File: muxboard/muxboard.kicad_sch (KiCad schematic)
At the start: 5 parts, among them U1 ADG426BNZ, U2 ADG426BNZ, U3 ADG426BNZ, U4 ADG1204YRUZ

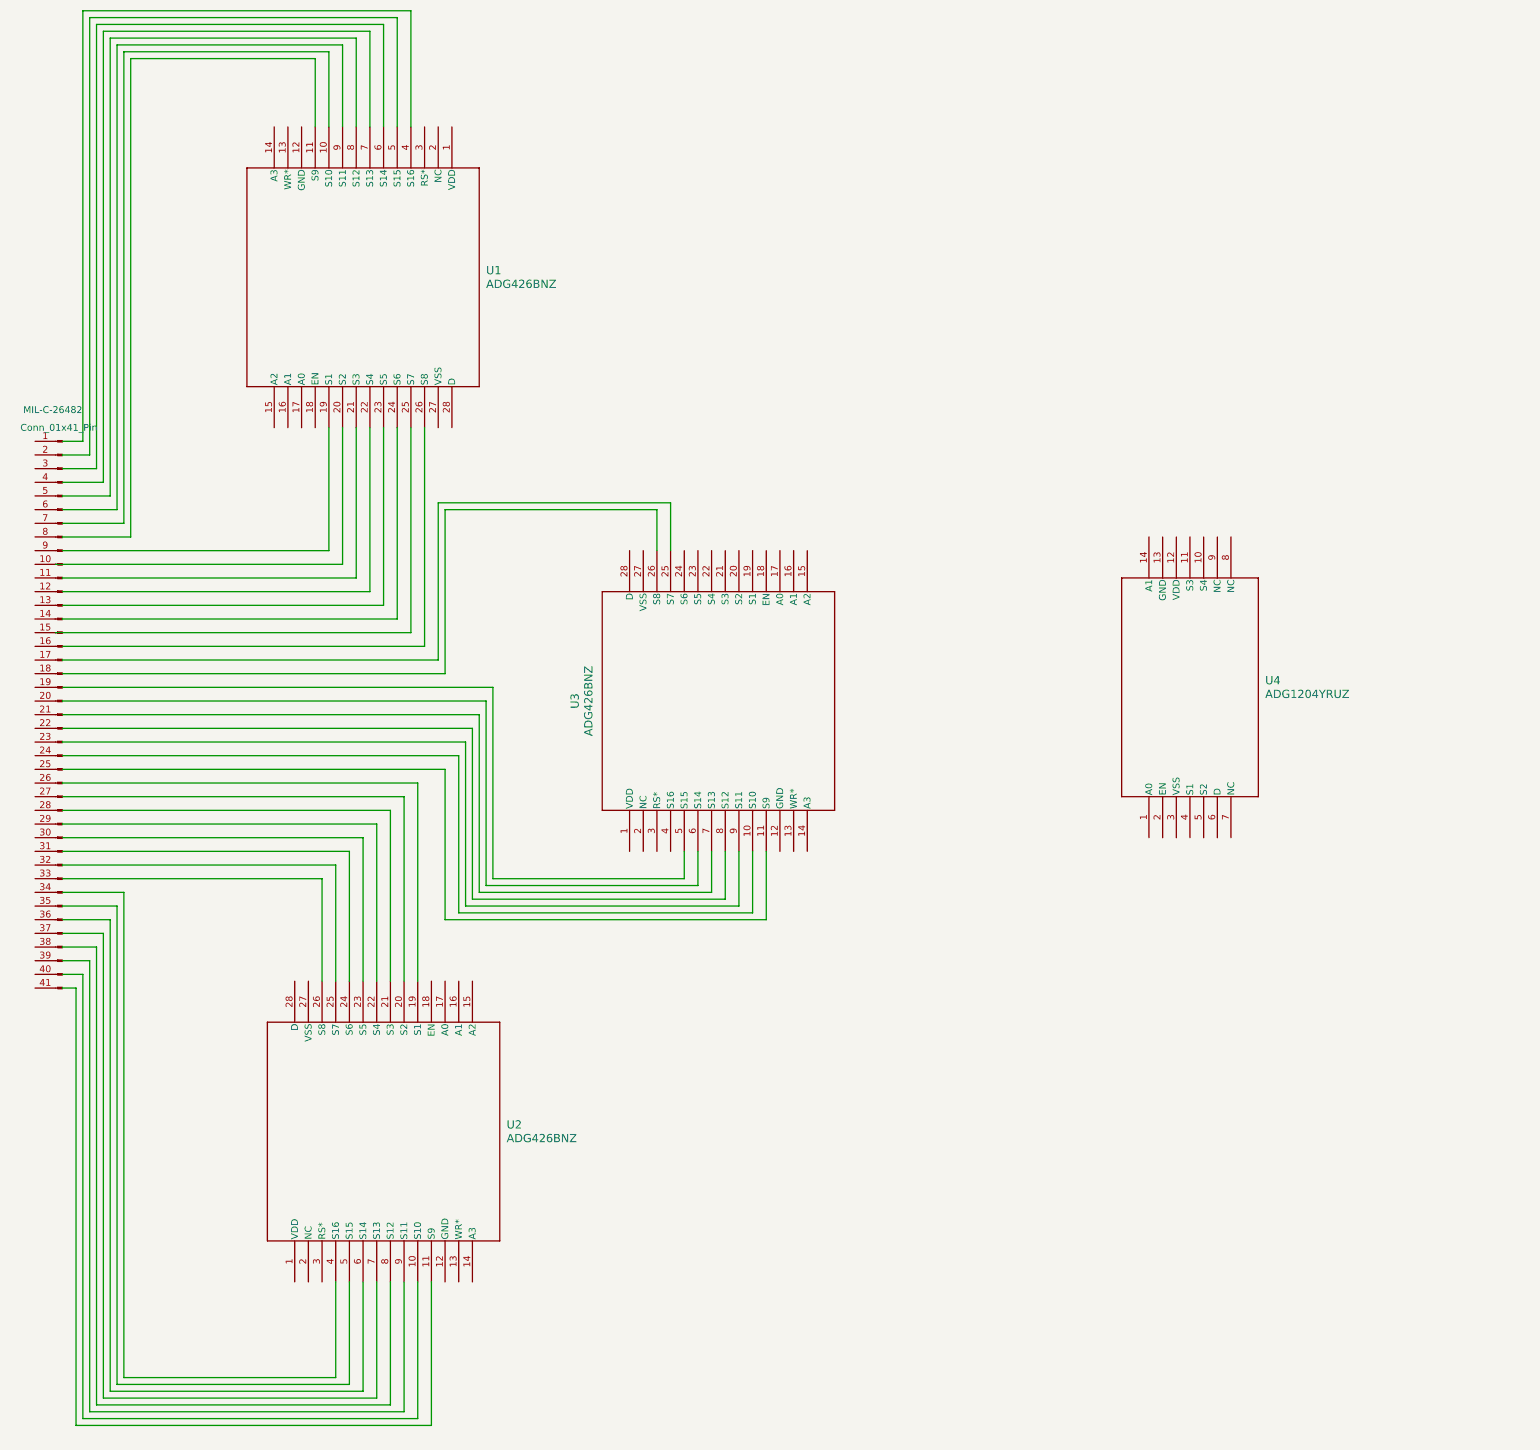
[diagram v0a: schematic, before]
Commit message: uploaded pcb terminal blocks; still need to connect and check wire connection
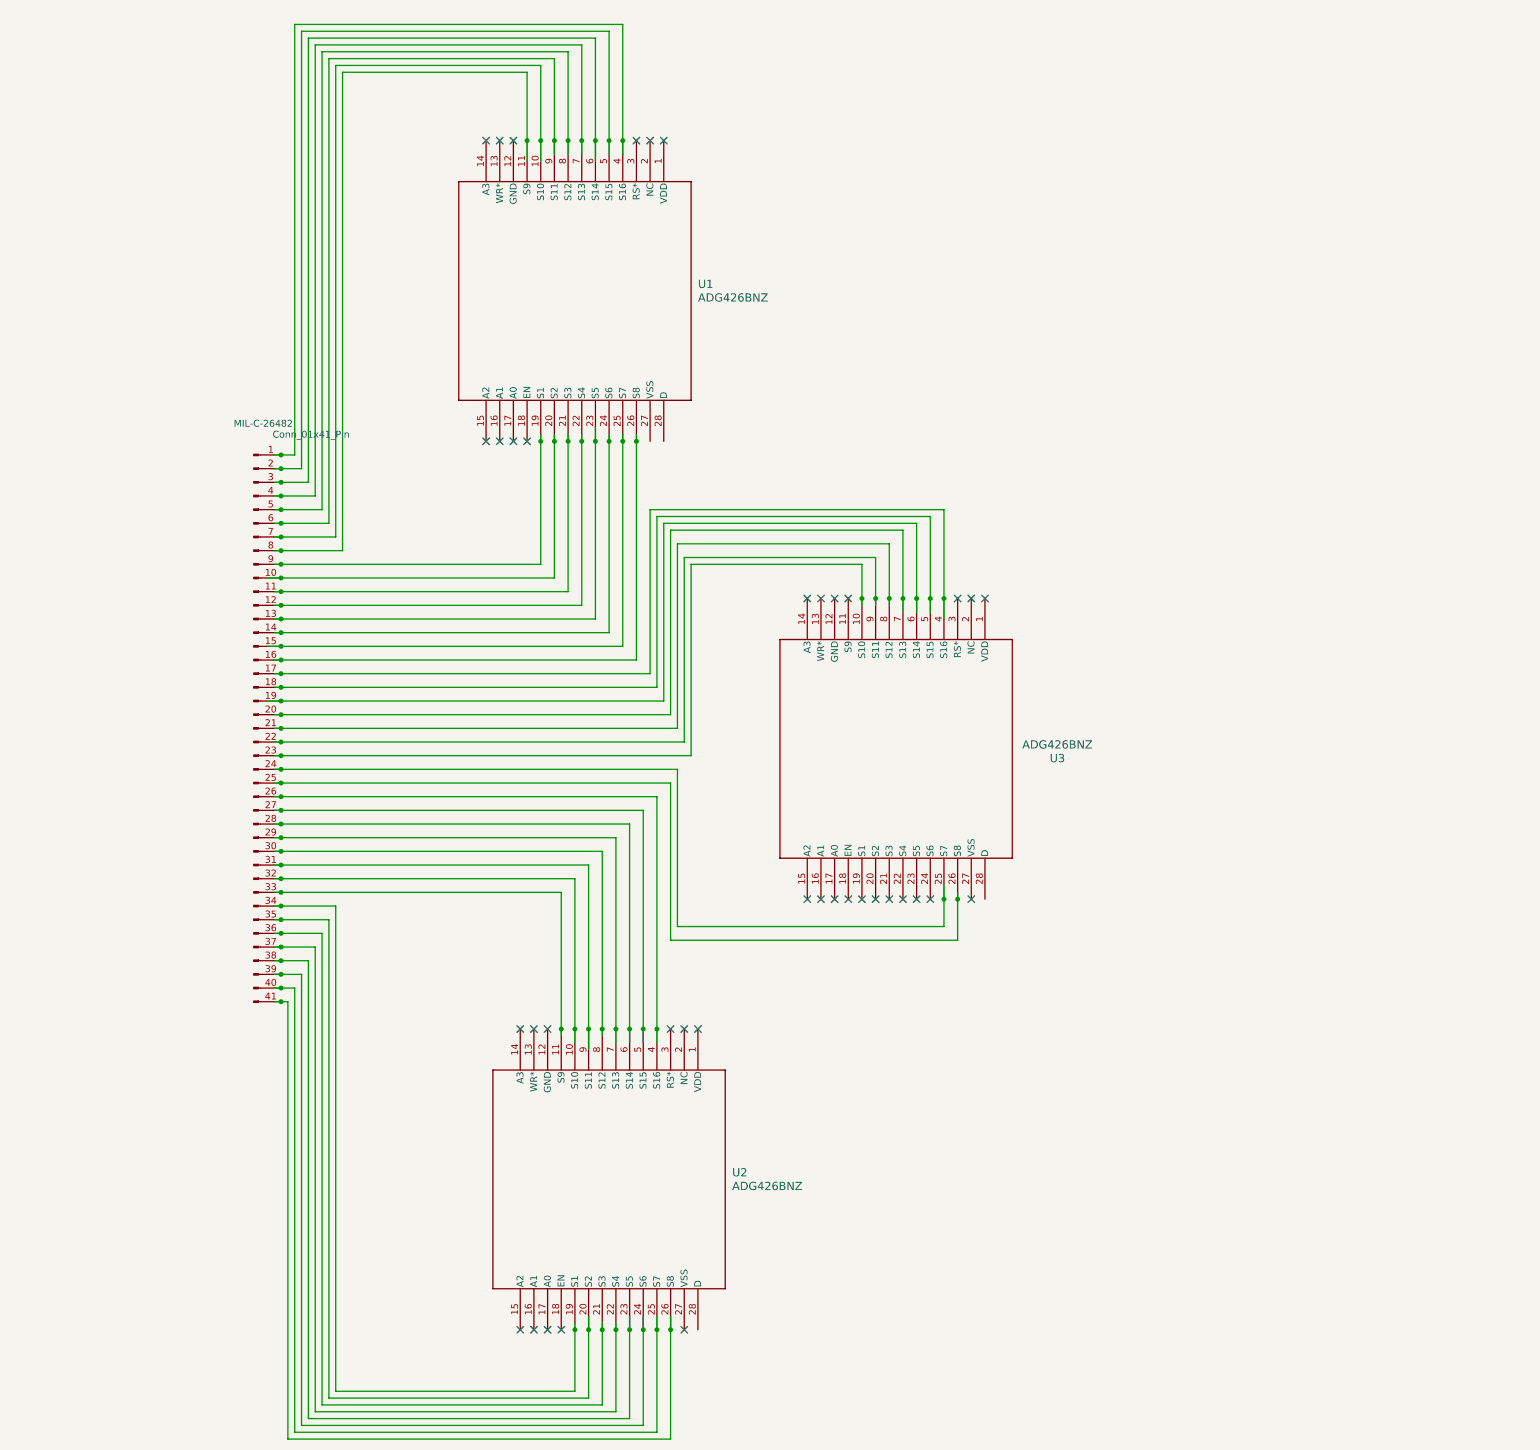
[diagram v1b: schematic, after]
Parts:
- removed U4: ADG1204YRUZ, RU_14_ADI, symbol ADG1204YRUZ:ADG1204YRUZ
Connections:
- net at MIL-C-26482.1 (Pin_1): now also U1.4 (S16)
- net at MIL-C-26482.10 (Pin_10): now also U1.20 (S2)
- net at MIL-C-26482.11 (Pin_11): now also U1.21 (S3)
- net at MIL-C-26482.12 (Pin_12): now also U1.22 (S4)
- net at MIL-C-26482.13 (Pin_13): now also U1.23 (S5)
- net at MIL-C-26482.14 (Pin_14): now also U1.24 (S6)
- net at MIL-C-26482.15 (Pin_15): now also U1.25 (S7)
- net at MIL-C-26482.16 (Pin_16): now also U1.26 (S8)
- net at MIL-C-26482.17 (Pin_17): now also U3.4 (S16)
- net at MIL-C-26482.18 (Pin_18): now also U3.5 (S15)
- net at MIL-C-26482.19 (Pin_19): now also U3.6 (S14)
- net at MIL-C-26482.2 (Pin_2): now also U1.5 (S15)
- net at MIL-C-26482.20 (Pin_20): now also U3.7 (S13)
- net at MIL-C-26482.21 (Pin_21): now also U3.8 (S12)
- net at MIL-C-26482.22 (Pin_22): now also U3.9 (S11)
- net at MIL-C-26482.23 (Pin_23): now also U3.10 (S10)
- net at MIL-C-26482.24 (Pin_24): now also U3.25 (S7)
- net at MIL-C-26482.25 (Pin_25): now also U3.26 (S8)
- net at MIL-C-26482.26 (Pin_26): now also U2.4 (S16)
- net at MIL-C-26482.27 (Pin_27): now also U2.5 (S15)
- net at MIL-C-26482.28 (Pin_28): now also U2.6 (S14)
- net at MIL-C-26482.29 (Pin_29): now also U2.7 (S13)
- net at MIL-C-26482.3 (Pin_3): now also U1.6 (S14)
- net at MIL-C-26482.30 (Pin_30): now also U2.8 (S12)
- net at MIL-C-26482.31 (Pin_31): now also U2.9 (S11)
- net at MIL-C-26482.32 (Pin_32): now also U2.10 (S10)
- net at MIL-C-26482.33 (Pin_33): now also U2.11 (S9)
- net at MIL-C-26482.34 (Pin_34): now also U2.19 (S1)
- net at MIL-C-26482.35 (Pin_35): now also U2.20 (S2)
- net at MIL-C-26482.36 (Pin_36): now also U2.21 (S3)
- net at MIL-C-26482.37 (Pin_37): now also U2.22 (S4)
- net at MIL-C-26482.38 (Pin_38): now also U2.23 (S5)
- net at MIL-C-26482.39 (Pin_39): now also U2.24 (S6)
- net at MIL-C-26482.4 (Pin_4): now also U1.7 (S13)
- net at MIL-C-26482.40 (Pin_40): now also U2.25 (S7)
- net at MIL-C-26482.41 (Pin_41): now also U2.26 (S8)
- net at MIL-C-26482.5 (Pin_5): now also U1.8 (S12)
- net at MIL-C-26482.6 (Pin_6): now also U1.9 (S11)
- net at MIL-C-26482.7 (Pin_7): now also U1.10 (S10)
- net at MIL-C-26482.8 (Pin_8): now also U1.11 (S9)
- net at MIL-C-26482.9 (Pin_9): now also U1.19 (S1)
- no-connect marks 0 -> 39
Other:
- moved on the sheet: MIL-C-26482, U1, U2, U3

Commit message: uploaded 3-pole terminal block; schematic rough draft is finished; left to do: - run ERC checks with connections - make sure all connections are properly aligned - ensure wire layout is feasible
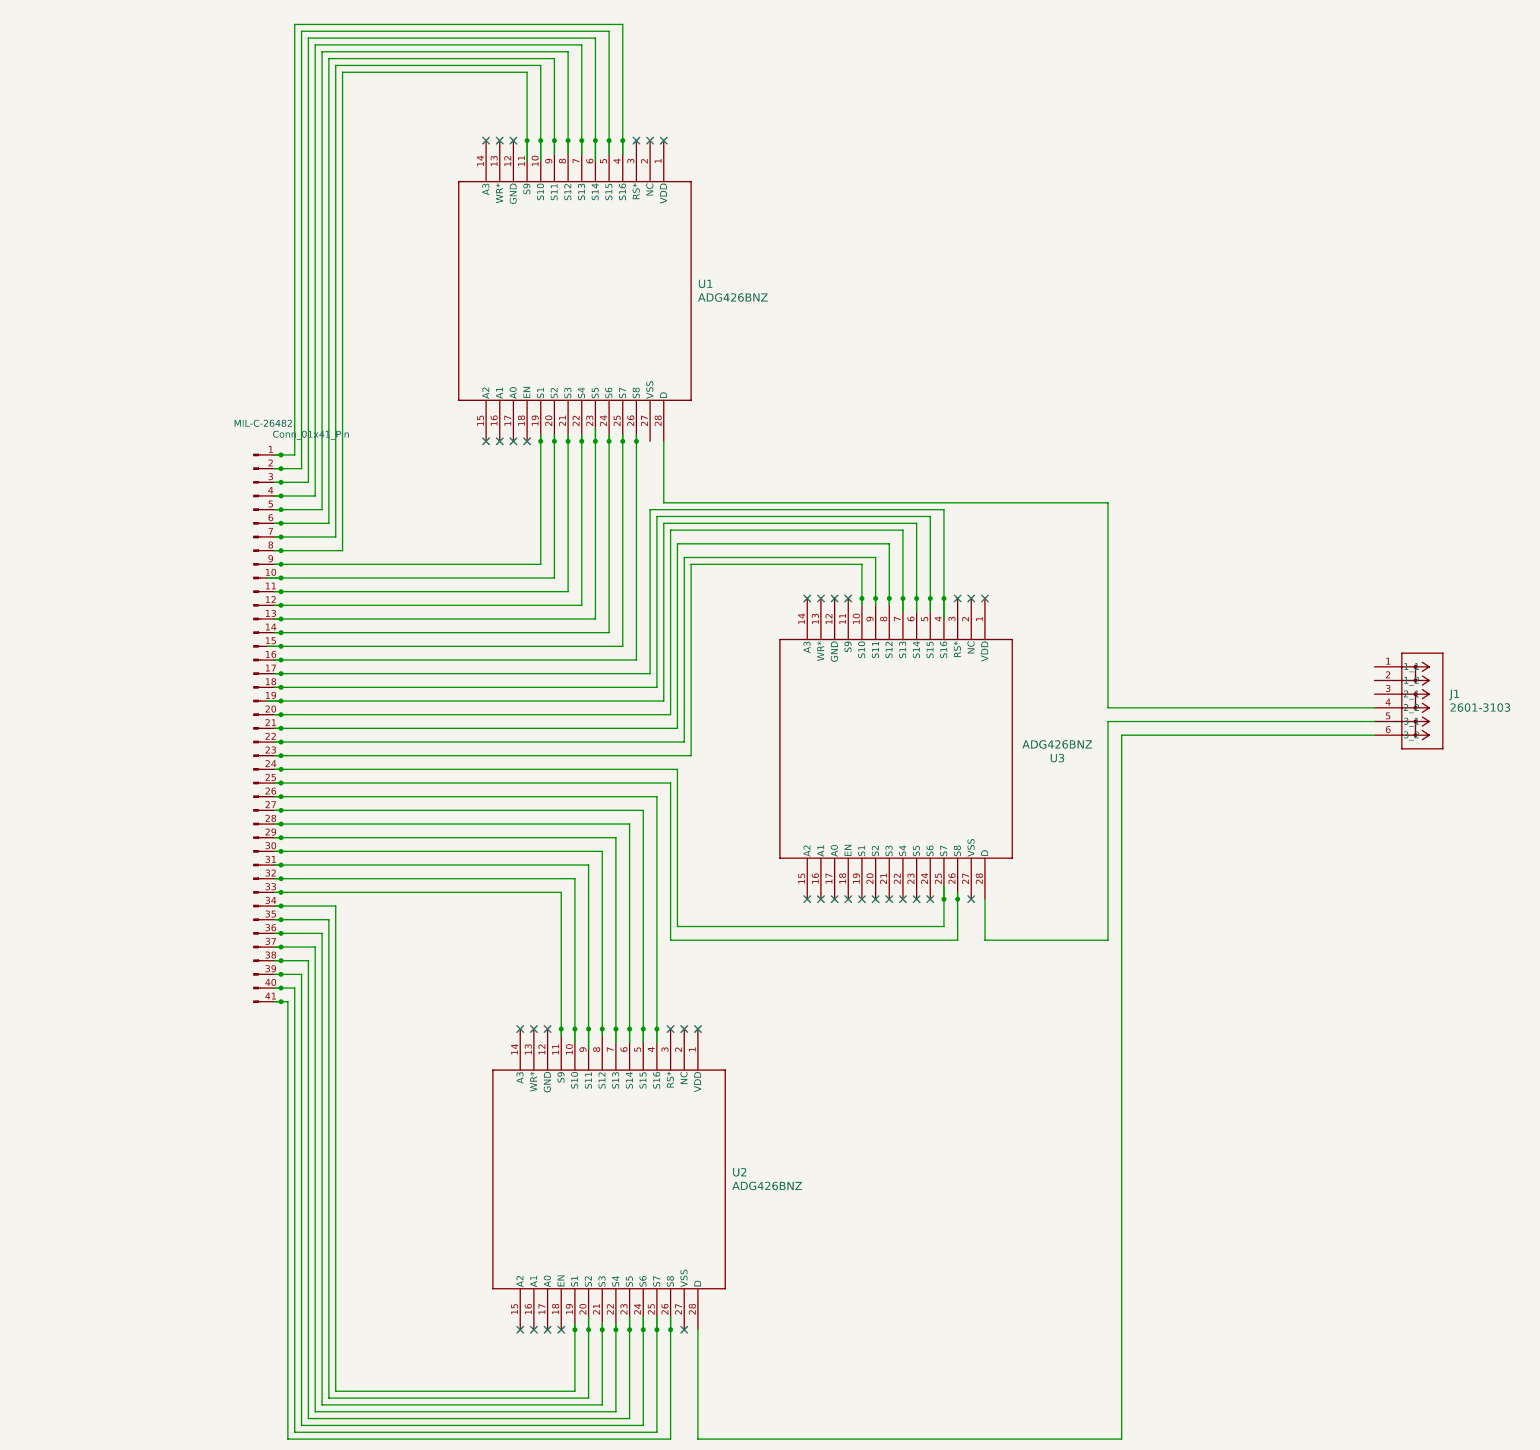
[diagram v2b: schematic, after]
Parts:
- added J1: 2601-3103, CONN3_2601-3103_WAG, symbol terminal block 3-pin:2601-3103
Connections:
- net at U1.28 (D): now also J1.4 (2_2)
- net at U2.28 (D): now also J1.6 (3_2)
- net at U3.28 (D): now also J1.5 (3_1)
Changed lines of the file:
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@@
+	(wire
+		(pts
+			(xy 251.46 146.05) (xy 300.99 146.05)
+		)
+		(stroke
+			(width 0)
+			(type default)
+		)
+	)
 	(wire
 		(pts
@@
 	(wire
 		(pts
+			(xy 254 148.59) (xy 300.99 148.59)
+		)
+		(stroke
+			(width 0)
+			(type default)
+		)
+	)
+	(wire
+		(pts
 			(xy 151.13 93.98) (xy 151.13 121.92)
 		)
@@
 	(wire
 		(pts
+			(xy 168.91 93.98) (xy 168.91 105.41)
+		)
+		(stroke
+			(width 0)
+			(type default)
+		)
+	)
+	(wire
+		(pts
 			(xy 102.87 19.05) (xy 156.21 19.05)
 		)
@@
 	(wire
 		(pts
+			(xy 228.6 179.07) (xy 228.6 186.69)
+		)
+		(stroke
+			(width 0)
+			(type default)
+		)
+	)
+	(wire
+		(pts
 			(xy 158.75 92.71) (xy 158.75 93.98)
 		)
@@
 	(wire
 		(pts
+			(xy 175.26 279.4) (xy 254 279.4)
+		)
+		(stroke
+			(width 0)
+			(type default)
+		)
+	)
+	(wire
+		(pts
 			(xy 158.75 38.1) (xy 158.75 40.64)
 		)
@@
 	(wire
 		(pts
+			(xy 168.91 105.41) (xy 251.46 105.41)
+		)
+		(stroke
+			(width 0)
+			(type default)
+		)
+	)
+	(wire
+		(pts
 			(xy 104.14 274.32) (xy 160.02 274.32)
 		)
@@
 	(wire
 		(pts
+			(xy 254 148.59) (xy 254 279.4)
+		)
+		(stroke
+			(width 0)
+			(type default)
+		)
+	)
+	(wire
+		(pts
 			(xy 162.56 165.1) (xy 162.56 203.2)
 		)
@@
 	(wire
 		(pts
+			(xy 228.6 186.69) (xy 251.46 186.69)
+		)
+		(stroke
+			(width 0)
+			(type default)
+		)
+	)
+	(wire
+		(pts
 			(xy 156.21 38.1) (xy 156.21 41.91)
 		)
@@
 	(wire
 		(pts
+			(xy 251.46 105.41) (xy 251.46 143.51)
+		)
+		(stroke
+			(width 0)
+			(type default)
+		)
+	)
+	(wire
+		(pts
 			(xy 96.52 99.06) (xy 97.79 99.06)
 		)
@@
 	(wire
 		(pts
+			(xy 251.46 143.51) (xy 300.99 143.51)
+		)
+		(stroke
+			(width 0)
+			(type default)
+		)
+	)
+	(wire
+		(pts
 			(xy 153.67 92.71) (xy 153.67 93.98)
 		)
@@
 		(pts
 			(xy 170.18 110.49) (xy 213.36 110.49)
+		)
+		(stroke
+			(width 0)
+			(type default)
+		)
+	)
+	(wire
+		(pts
+			(xy 175.26 279.4) (xy 175.26 259.08)
+		)
+		(stroke
+			(width 0)
+			(type default)
+		)
+	)
+	(wire
+		(pts
+			(xy 251.46 186.69) (xy 251.46 146.05)
 		)
 		(stroke
@@
 					(unit 1)
 				)
+			)
+		)
+	)
+	(symbol
+		(lib_id "terminal block 3-pin:2601-3103")
+		(at 300.99 135.89 0)
+		(unit 1)
+		(exclude_from_sim no)
+		(in_bom yes)
+		(on_board yes)
+		(dnp no)
+		(fields_autoplaced yes)
+		(property "Reference" "J1"
+			(at 314.96 140.9699 0)
+			(effects
+				(font
+					(size 1.524 1.524)
+				)
+				(justify left)
+			)
+		)
+		(property "Value" "2601-3103"
+			(at 314.96 143.5099 0)
+			(effects
+				(font
+					(size 1.524 1.524)
+				)
+				(justify left)
+			)
+		)
+		(property "Footprint" "CONN3_2601-3103_WAG"
+			(at 300.99 135.89 0)
+			(effects
+				(font
+					(size 1.27 1.27)
+					(italic yes)
+				)
+				(hide yes)
+			)
+		)
+		(property "Datasheet" "2601-3103"
+			(at 300.99 135.89 0)
+			(effects
+				(font
+					(size 1.27 1.27)
+					(italic yes)
+				)
+				(hide yes)
+			)
+		)
+		(property "Description" ""
+			(at 300.99 135.89 0)
+			(effects
+				(font
+					(size 1.27 1.27)
+				)
+				(hide yes)
+			)
+		)
+		(pin "4"
+		)
+		(pin "5"
+		)
+		(pin "3"
+		)
+		(pin "6"
+		)
+		(pin "1"
+		)
+		(pin "2"
+		)
+		(instances
+			(project ""
+				(path "/29ffdad2-b01b-4d38-a314-2321b1ddbbf7"
+					(reference "J1")
+					(unit 1)
+				)
